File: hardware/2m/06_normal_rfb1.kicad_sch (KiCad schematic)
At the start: 16 parts, among them J501 NORMAL 50ohm SMA

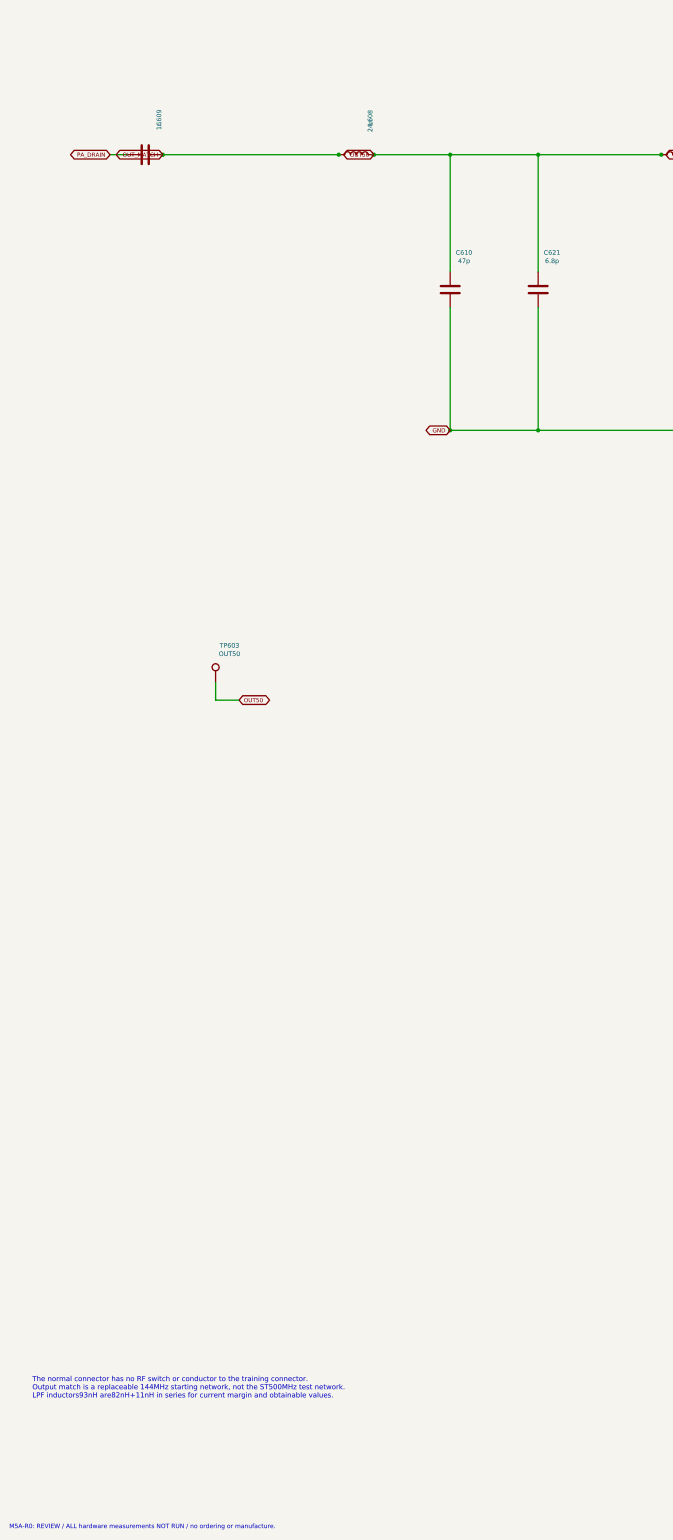
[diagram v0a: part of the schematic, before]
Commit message: Preserve M5A-R1 VHF electrical candidate and review evidence
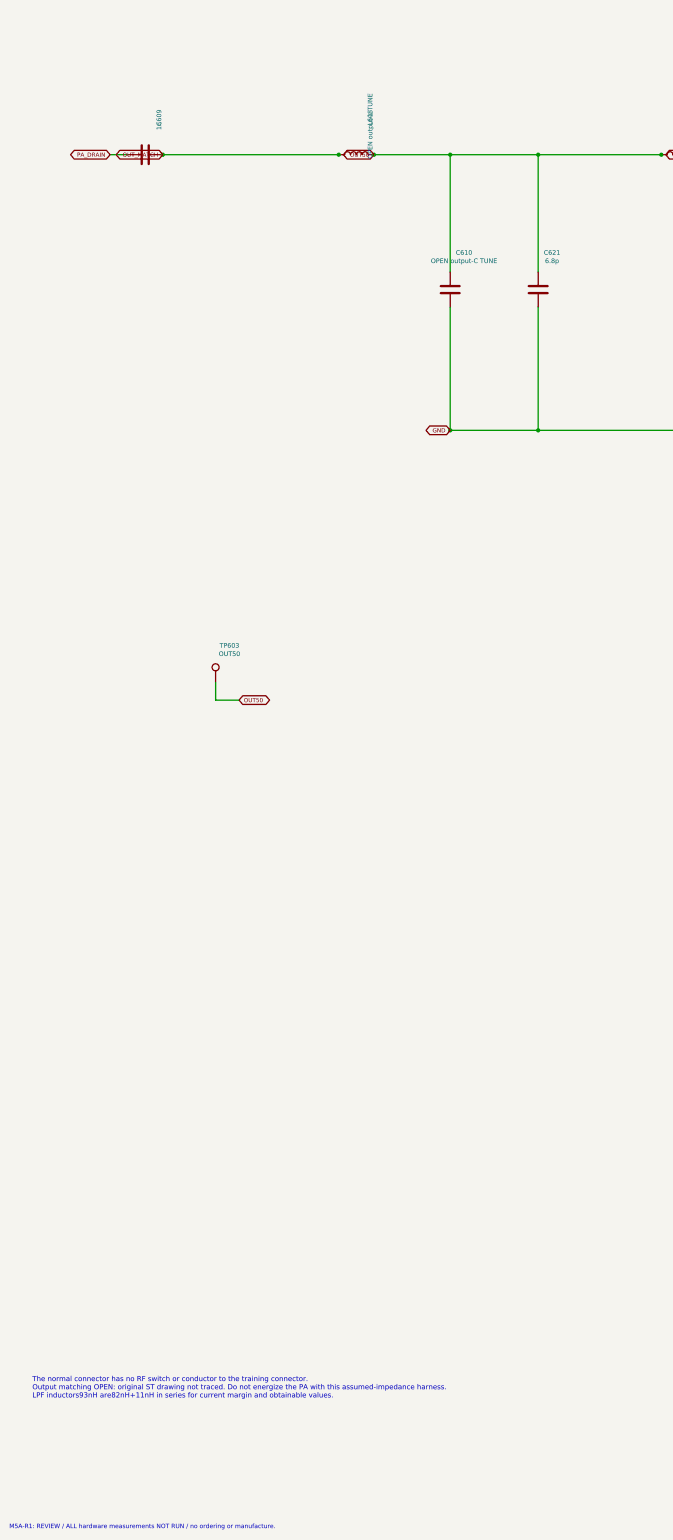
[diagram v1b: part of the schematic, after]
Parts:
- C610: value 47p -> OPEN output-C TUNE; Engineering_Note Calculated10ohm target with38pF Coss gives24.5nH/47.2pF; se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 -> OPEN: actual ST output-match topology not retrieved. Empty 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; MPN OPEN: C0G100V 47p -> OPEN: OPEN output-C TUNE voltage/ESR qualification
- L608: value 24n -> OPEN output-L TUNE; MPN 0805CS-240XJRC -> OPEN: RF tuning inductor OPEN output-L TUNE
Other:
- note added: "M5A-R1: REVIEW / ALL hardware measurements NOT RUN / no ordering or manufacture."
- note added: "The normal connector has no RF switch or conductor to the training connector. Output matching OPEN: original ST drawing not traced. Do not energize the PA with this assumed-impedance harness. LPF inductors93nH are82nH+11nH in series for current margin and obtainable values."
- note removed: "M5A-R0: REVIEW / ALL hardware measurements NOT RUN / no ordering or manufacture."
- note removed: "The normal connector has no RF switch or conductor to the training connector. Output match is a replaceable 144MHz starting network, not the ST500MHz test network. LPF inductors93nH are82nH+11nH in series for current margin and obtainable values."
